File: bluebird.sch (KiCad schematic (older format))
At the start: 32 parts, among them J1 USB_C_Receptacle_USB2.0, J3 Conn_01x05, J4 Conn_01x01, J5 Conn_01x01, SW1 SW_PUSH, U1 ATMEGA32U4, U2 MCP23017_SS, U3 IS31FL3731-SA, Y1 FA328 16MHz

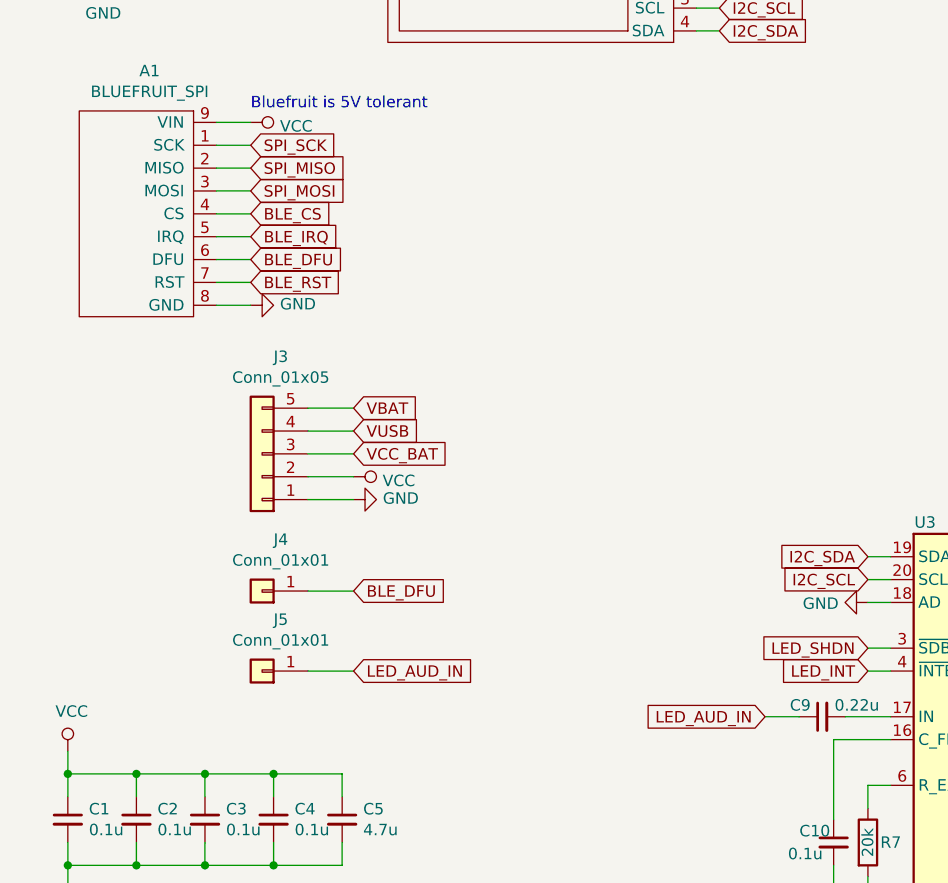
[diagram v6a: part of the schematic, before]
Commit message: Wire ISP/USB to debug headers
Change L1 footprint
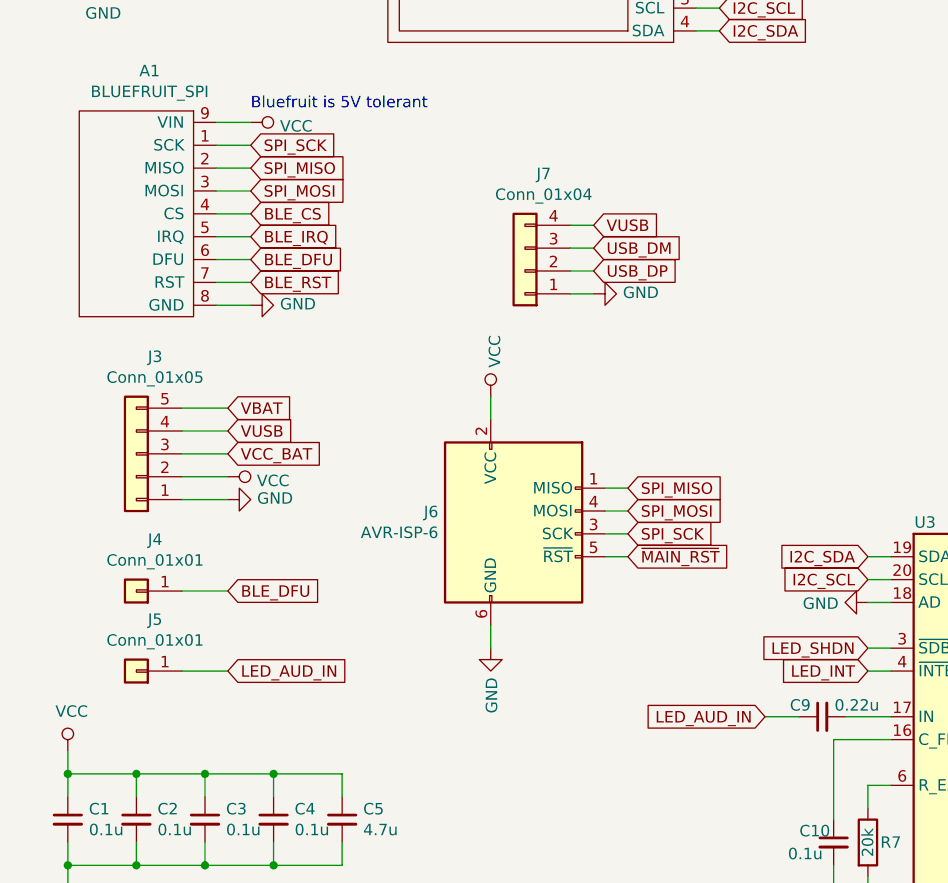
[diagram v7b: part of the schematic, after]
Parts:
- added J6: AVR-ISP-6, bluebird:AVR_ISP6, symbol Connector:AVR-ISP-6
- added J7: Conn_01x04, Connector_PinHeader_2.54mm:PinHeader_1x04_P2.54mm_Vertical, symbol Connector_Generic:Conn_01x04
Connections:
- net GND: now also J6.6 (GND), J7.1 (Pin_1)
- net SPI_MISO: now also J6.1 (MISO)
- net SPI_MOSI: now also J6.4 (MOSI)
- net SPI_SCK: now also J6.3 (SCK)
- net USB_DM: now also J7.3 (Pin_3)
- net USB_DP: now also J7.2 (Pin_2)
- net VCC: now also J6.2 (VCC)
- net VUSB: now also J7.4 (Pin_4)
- net ~MAIN_RST: now also J6.5 (~RST)
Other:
- moved on the sheet: J3, J4, J5
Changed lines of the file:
@@
 L power:GND #PWR0107
 U 1 1 6354D201
-P 2050 5050
-F 0 "#PWR0107" H 2050 4800 50  0001 C CNN
-F 1 "GND" V 2055 4922 50  0000 R CNN
-F 2 "" H 2050 5050 50  0001 C CNN
-F 3 "" H 2050 5050 50  0001 C CNN
-	1    2050 5050
+P 1500 5050
+F 0 "#PWR0107" H 1500 4800 50  0001 C CNN
+F 1 "GND" V 1505 4922 50  0000 R CNN
+F 2 "" H 1500 5050 50  0001 C CNN
+F 3 "" H 1500 5050 50  0001 C CNN
+	1    1500 5050
 	0    -1   -1   0
 $EndComp
@@
 L power:VCC #PWR0108
 U 1 1 6354DC23
-P 2050 4950
-F 0 "#PWR0108" H 2050 4800 50  0001 C CNN
-F 1 "VCC" V 2068 5077 50  0000 L CNN
-F 2 "" H 2050 4950 50  0001 C CNN
-F 3 "" H 2050 4950 50  0001 C CNN
-	1    2050 4950
-	0    1    1    0
-$EndComp
-Text GLabel 2050 4750 2    50   Input ~ 0
+P 1500 4950
+F 0 "#PWR0108" H 1500 4800 50  0001 C CNN
+F 1 "VCC" V 1518 5077 50  0000 L CNN
+F 2 "" H 1500 4950 50  0001 C CNN
+F 3 "" H 1500 4950 50  0001 C CNN
+	1    1500 4950
+	0    1    1    0
+$EndComp
+Text GLabel 1500 4750 2    50   Input ~ 0
 VUSB
-Text GLabel 2050 4650 2    50   Input ~ 0
+Text GLabel 1500 4650 2    50   Input ~ 0
 VBAT
-Text GLabel 2050 4850 2    50   Input ~ 0
+Text GLabel 1500 4850 2    50   Input ~ 0
 VCC_BAT
 Wire Wire Line
-	1850 4650 2050 4650
-Wire Wire Line
-	1850 4750 2050 4750
-Wire Wire Line
-	1850 4850 2050 4850
-Wire Wire Line
-	1850 4950 2050 4950
-Wire Wire Line
-	1850 5050 2050 5050
+	1300 4650 1500 4650
+Wire Wire Line
+	1300 4750 1500 4750
+Wire Wire Line
+	1300 4850 1500 4850
+Wire Wire Line
+	1300 4950 1500 4950
+Wire Wire Line
+	1300 5050 1500 5050
 $Comp
 L Connector_Generic:Conn_01x05 J3
 U 1 1 5E871C97
-P 1650 4850
-F 0 "J3" H 1568 4425 50  0000 C CNN
-F 1 "Conn_01x05" H 1568 4516 50  0000 C CNN
-F 2 "Connector_PinHeader_2.54mm:PinHeader_1x05_P2.54mm_Vertical" H 1650 4850 50  0001 C CNN
-F 3 "~" H 1650 4850 50  0001 C CNN
-	1    1650 4850
+P 1100 4850
+F 0 "J3" H 1018 4425 50  0000 C CNN
+F 1 "Conn_01x05" H 1018 4516 50  0000 C CNN
+F 2 "Connector_PinHeader_2.54mm:PinHeader_1x05_P2.54mm_Vertical" H 1100 4850 50  0001 C CNN
+F 3 "~" H 1100 4850 50  0001 C CNN
+	1    1100 4850
 	-1   0    0    1
 $EndComp
@@
 L Connector_Generic:Conn_01x01 J4
 U 1 1 5E9FC31F
-P 1650 5450
-F 0 "J4" H 1568 5225 50  0000 C CNN
-F 1 "Conn_01x01" H 1568 5316 50  0000 C CNN
-F 2 "Connector_PinHeader_2.54mm:PinHeader_1x01_P2.54mm_Vertical" H 1650 5450 50  0001 C CNN
-F 3 "~" H 1650 5450 50  0001 C CNN
-	1    1650 5450
-	-1   0    0    1
-$EndComp
-Text GLabel 2050 5450 2    50   Input ~ 0
+P 1100 5450
+F 0 "J4" H 1018 5225 50  0000 C CNN
+F 1 "Conn_01x01" H 1018 5316 50  0000 C CNN
+F 2 "Connector_PinHeader_2.54mm:PinHeader_1x01_P2.54mm_Vertical" H 1100 5450 50  0001 C CNN
+F 3 "~" H 1100 5450 50  0001 C CNN
+	1    1100 5450
+	-1   0    0    1
+$EndComp
+Text GLabel 1500 5450 2    50   Input ~ 0
 BLE_DFU
 Wire Wire Line
-	2050 5450 1850 5450
+	1500 5450 1300 5450
 $Comp
 L Connector_Generic:Conn_01x01 J5
 U 1 1 5EA0F98E
-P 1650 5800
-F 0 "J5" H 1568 5575 50  0000 C CNN
-F 1 "Conn_01x01" H 1568 5666 50  0000 C CNN
-F 2 "Connector_PinHeader_2.54mm:PinHeader_1x01_P2.54mm_Vertical" H 1650 5800 50  0001 C CNN
-F 3 "~" H 1650 5800 50  0001 C CNN
-	1    1650 5800
-	-1   0    0    1
-$EndComp
-Text GLabel 2050 5800 2    50   Input ~ 0
+P 1100 5800
+F 0 "J5" H 1018 5575 50  0000 C CNN
+F 1 "Conn_01x01" H 1018 5666 50  0000 C CNN
+F 2 "Connector_PinHeader_2.54mm:PinHeader_1x01_P2.54mm_Vertical" H 1100 5800 50  0001 C CNN
+F 3 "~" H 1100 5800 50  0001 C CNN
+	1    1100 5800
+	-1   0    0    1
+$EndComp
+Text GLabel 1500 5800 2    50   Input ~ 0
 LED_AUD_IN
 Wire Wire Line
-	1850 5800 2050 5800
+	1300 5800 1500 5800
 $Comp
 L custom:SSD1306 A2
@@
 	2150 7050 2150 7100
 Connection ~ 2150 7100
+$Comp
+L Connector:AVR-ISP-6 J6
+U 1 1 5E76A6EE
+P 2750 5200
+F 0 "J6" H 2421 5296 50  0000 R CNN
+F 1 "AVR-ISP-6" H 2421 5205 50  0000 R CNN
+F 2 "bluebird:AVR_ISP6" V 2500 5250 50  0001 C CNN
+F 3 " ~" H 1475 4650 50  0001 C CNN
+	1    2750 5200
+	1    0    0    -1
+$EndComp
+Text GLabel 3250 5200 2    50   Input ~ 0
+SPI_SCK
+Text GLabel 3250 5100 2    50   Input ~ 0
+SPI_MOSI
+Text GLabel 3250 5000 2    50   Input ~ 0
+SPI_MISO
+Text GLabel 3250 5300 2    50   Input ~ 0
+~MAIN_RST
+Wire Wire Line
+	3150 5300 3250 5300
+Wire Wire Line
+	3150 5200 3250 5200
+Wire Wire Line
+	3150 5100 3250 5100
+Wire Wire Line
+	3150 5000 3250 5000
+$Comp
+L power:GND #PWR038
+U 1 1 5E7C018A
+P 2650 5700
+F 0 "#PWR038" H 2650 5450 50  0001 C CNN
+F 1 "GND" V 2655 5572 50  0000 R CNN
+F 2 "" H 2650 5700 50  0001 C CNN
+F 3 "" H 2650 5700 50  0001 C CNN
+	1    2650 5700
+	1    0    0    -1
+$EndComp
+$Comp
+L power:VCC #PWR032
+U 1 1 5E7C04E1
+P 2650 4600
+F 0 "#PWR032" H 2650 4450 50  0001 C CNN
+F 1 "VCC" V 2668 4727 50  0000 L CNN
+F 2 "" H 2650 4600 50  0001 C CNN
+F 3 "" H 2650 4600 50  0001 C CNN
+	1    2650 4600
+	1    0    0    -1
+$EndComp
+Wire Wire Line
+	2650 4600 2650 4700
+Wire Wire Line
+	2650 5700 2650 5600
+Text GLabel 3100 4050 2    50   Input ~ 0
+USB_DP
+Text GLabel 3100 3950 2    50   Input ~ 0
+USB_DM
+Wire Wire Line
+	3000 3950 3100 3950
+Wire Wire Line
+	3000 4050 3100 4050
+$Comp
+L Connector_Generic:Conn_01x04 J7
+U 1 1 5E80E845
+P 2800 4050
+F 0 "J7" H 2718 3625 50  0000 C CNN
+F 1 "Conn_01x04" H 2718 3716 50  0000 C CNN
+F 2 "Connector_PinHeader_2.54mm:PinHeader_1x04_P2.54mm_Vertical" H 2800 4050 50  0001 C CNN
+F 3 "~" H 2800 4050 50  0001 C CNN
+	1    2800 4050
+	-1   0    0    1
+$EndComp
+$Comp
+L power:GND #PWR039
+U 1 1 5E80FF84
+P 3100 4150
+F 0 "#PWR039" H 3100 3900 50  0001 C CNN
+F 1 "GND" V 3105 4022 50  0000 R CNN
+F 2 "" H 3100 4150 50  0001 C CNN
+F 3 "" H 3100 4150 50  0001 C CNN
+	1    3100 4150
+	0    -1   -1   0
+$EndComp
+Wire Wire Line
+	3000 3850 3100 3850
+Text GLabel 3100 3850 2    50   Input ~ 0
+VUSB
+Wire Wire Line
+	3000 4150 3100 4150
 $EndSCHEMATC

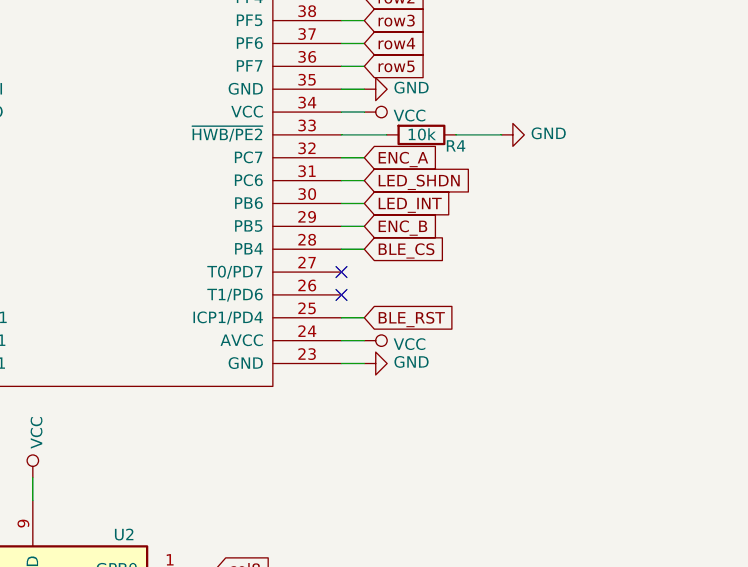
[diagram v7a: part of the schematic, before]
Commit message: Add wiring for battery indication
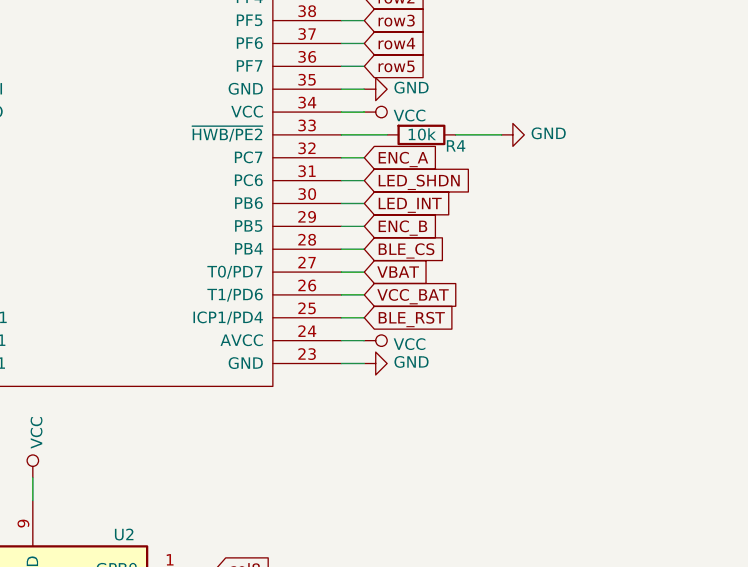
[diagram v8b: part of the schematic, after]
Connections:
- net VBAT: now also U1.27 (T0/PD7)
- net VCC_BAT: now also U1.26 (T1/PD6)
- no-connect marks 15 -> 13
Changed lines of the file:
@@
 NoConn ~ 7150 3100
 NoConn ~ 7150 3200
-NoConn ~ 9300 2900
-NoConn ~ 9300 2800
 NoConn ~ 9300 1300
 NoConn ~ 7250 4700
@@
 Wire Wire Line
 	3000 4150 3100 4150
+Text GLabel 9400 2800 2    50   Input ~ 0
+VBAT
+Wire Wire Line
+	9300 2800 9400 2800
+Text GLabel 9400 2900 2    50   Input ~ 0
+VCC_BAT
+Wire Wire Line
+	9300 2900 9400 2900
 $EndSCHEMATC
